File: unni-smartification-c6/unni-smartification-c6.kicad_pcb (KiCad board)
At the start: 2 copper layers, 83.3 x 65 mm, 73 parts, among them J1 USB-C (replacement daughterbo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, J10 UART TEST, J2 Li-Ion 1S JST-PH, J20 CO2 tap: SDA/SCL/GND, J21 RT/RH tap: RT/RH/GND, J22 TOUCH / LED+ / LED- / GND, J4 UNNI DC / battery input - AC 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, Q1 AO3401A, Q10 AO3400A touch emulator, Q2 AO3401A, Q3 AO3400A, Q4 AO3400A, U1 MCP73831T-2ACI/OT, U10 ESP32-C6-MINI-1, U2 TPS63031DSK, U3 TPS613222ADBZ (5V)

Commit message: trying routing the usb-pcb
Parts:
- added U4: USBLC6-2SC6, Package_TO_SOT_SMD:SOT-23-6, B.Cu at (0.00, 0.00)
- D1, D3, D4: footprint Diode_SMD:D_SMA -> Diode_SMD:D_SMA_Handsoldering
- Q1, Q10, Q2, Q3, Q4, U3: footprint Package_TO_SOT_SMD:SOT-23 -> Package_TO_SOT_SMD:SOT-23_Handsoldering
- U1: footprint Package_TO_SOT_SMD:SOT-23-5 -> Package_TO_SOT_SMD:SOT-23-5_HandSoldering
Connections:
- J1 pad A6: USB_RAW_P -> USB_P
- J1 pad A7: USB_RAW_N -> USB_N
- J1 pad B6: USB_RAW_P -> USB_P
- J1 pad B7: USB_RAW_N -> USB_N
- J2 pad 1: +BATT -> GND
- J2 pad 2: GND -> +BATT
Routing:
- net VBUS: track 0.00 -> 17.4 mm, vias 0 -> 14
- net Net-(Q3-G): track 0.00 -> 10.6 mm
- net SYS: track 0.00 -> 10.6 mm, vias 0 -> 2
- net USB_N: track 0.00 -> 9.54 mm
- net USB_P: track 0.00 -> 8.87 mm
- net +BATT: track 0.00 -> 8.37 mm, vias 0 -> 14
- net Net-(Q2-G): track 0.00 -> 7.80 mm
- net /USB + Power/BOOST_IN: track 0.00 -> 7.66 mm, vias 0 -> 6
- net Net-(Q1-G): track 0.00 -> 7.54 mm
- net +3V3: track 0.00 -> 4.00 mm, vias 0 -> 2
- net GND: track 0.00 -> 3.67 mm, vias 0 -> 22
- net Net-(U1-PROG): track 0.00 -> 2.22 mm
- net Net-(J1-CC1): track 7.64 -> 9.80 mm
- net Net-(J1-CC2): track 7.39 -> 9.43 mm
- net Net-(U1-STAT): track 0.00 -> 1.97 mm
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- added copper zone on B.Cu, net +BATT
- added copper zone on F.Cu, net +BATT
- added copper zone on B.Cu, net /USB + Power/BOOST_IN
- added copper zone on F.Cu, net Net-(U2-L1)
- added copper zone on F.Cu, net Net-(U2-L2)
- added copper zone on F.Cu, net Net-(U3-SW)
- added copper zone on B.Cu, net SYS
- added copper zone on B.Cu, net VBUS
- added copper zone on F.Cu, net VBUS

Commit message: add usb-esp and finalize usb-pcb
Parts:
- added C14: 100n, Capacitor_SMD:C_0603_1608Metric_Pad1.08x0.95mm_HandSolder, B.Cu at (0.00, 0.00)
- C9: moved to B.Cu
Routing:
- net +BATT: track 8.37 -> 0.00 mm, vias 14 -> 13
- net Net-(Q2-G): track 7.80 -> 0.00 mm
- net /USB + Power/BOOST_IN: track 7.66 -> 0.00 mm, vias 6 -> 12
- net UNNI_AC: track 0.00 -> 3.54 mm, vias 0 -> 1
- net Net-(Q3-G): track 10.6 -> 13.8 mm
- net GND: track 3.67 -> 6.22 mm, vias 22 -> 38
- net VBUS: track 17.4 -> 19.8 mm, vias 14 -> 20
- net Net-(J1-CC1): track 9.80 -> 11.0 mm
- net Net-(J1-CC2): track 9.43 -> 8.64 mm
- net USB_P: track 8.87 -> 8.15 mm
- added copper zone on In1.Cu, net GND
- added copper zone on In2.Cu, net GND
- added copper zone on F.Cu, net Net-(Q2-G)
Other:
- copper layers 2 -> 4

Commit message: move some power stuff to esp board, update some footprints
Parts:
- added SW1: RESET, Button_Switch_THT:SW_PUSH_6mm, F.Cu at (0.00, 0.00)
- added SW2: BOOT, Button_Switch_THT:SW_PUSH_6mm, F.Cu at (0.00, 0.00)
- C9: moved to F.Cu
- J2: footprint Connector_JST:JST_PH_S2B-PH-SM4-TB_1x02-1MP_P2.00mm_Horizontal -> Connector_JST:JST_PH_S2B-PH-K_1x02_P2.00mm_Horizontal
- L1: value 1.5uH -> 2.2uH
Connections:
- J4 pad 2: UNNI_AC -> GND
- J4 pad 3: GND -> UNNI_AC
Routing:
- net +BATT: track 0.00 -> 13.9 mm
- net SYS: track 10.9 -> 5.99 mm
- net UNNI_AC: track 3.54 -> 0.00 mm, vias 1 -> 0
- net Net-(Q1-G): track 7.76 -> 4.58 mm
- net VBUS: track 19.8 -> 21.2 mm, vias 20 -> 33
- net Net-(Q3-G): track 13.8 -> 12.5 mm, vias 0 -> 2
- net GND: track 6.22 -> 5.61 mm, vias 38 -> 51
- net /USB + Power/BOOST_IN: vias 12 -> 0
- added copper zone on F.Cu, net UNNI_AC

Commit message: re-do ESP PCB
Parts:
- removed J10: UART TEST, Connector_JST:JST_PH_S3B-PH-SM4-TB_1x03-1MP_P2.00mm_Horizontal
- removed J20: CO2 tap: SDA/SCL/GND, Connector_JST:JST_PH_S3B-PH-SM4-TB_1x03-1MP_P2.00mm_Horizontal
- removed J21: RT/RH tap: RT/RH/GND, Connector_JST:JST_PH_S3B-PH-SM4-TB_1x03-1MP_P2.00mm_Horizontal
- removed J22: TOUCH / LED+ / LED- / GND, Connector_JST:JST_PH_S4B-PH-SM4-TB_1x04-1MP_P2.00mm_Horizontal
- removed TP1: BACKLIGHT_LED_NEG, TestPoint:TestPoint_Pad_D1.0mm
- added J11, J24, J3: Conn_01x01, Connector_Wire:SolderWire-0.5sqmm_1x01_D0.9mm_OD2.1mm, F.Cu at (0.00, 0.00)
- added J12, J13, J14, J15, J17, J18, J19, J23, J25, J26, J27, J5, J6, J7, J8, J9: Conn_01x01, Connector_Wire:SolderWire-0.1sqmm_1x01_D0.4mm_OD1mm, F.Cu at (0.00, 0.00)
- L1: footprint Inductor_SMD:L_TDK_NLV32_3.2x2.5mm -> Unni_Inductor:L_Murata_LQH3NPN_3.0x3.0mm_HandSolder
- L2: footprint Inductor_SMD:L_TDK_NLV32_3.2x2.5mm -> Unni_Inductor:L_Murata_DFE322520FD_3.2x2.5mm_HandSolder
- RT1: footprint Resistor_THT:R_Axial_DIN0204_L3.6mm_D1.6mm_P5.08mm_Horizontal -> Connector_PinSocket_2.54mm:PinSocket_1x02_P2.54mm_Vertical
- SW1, SW2: footprint Button_Switch_THT:SW_PUSH_6mm -> Unni_Switch:SW_Jianfu_TVAF36-N014JW-R_HandSolder
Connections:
- net GND renamed CONN_GND
- net Net-(J22-Pin_1) renamed CONN_TOUCH
- net USB_N renamed USBPort_N
- net USB_P renamed USBPort_P
- net USB_RAW_N renamed CONN_USB_N
- net USB_RAW_P renamed CONN_USB_P
- net VBUS renamed CONN_VBUS
- R40 pad 1: Net-(J20-Pin_1) -> CONN_SDA
- R41 pad 1: Net-(J20-Pin_2) -> CONN_SCL
- R42 pad 1: Net-(J21-Pin_1) -> CONN_RT
- R43 pad 1: Net-(J21-Pin_2) -> CONN_RH
- R50 pad 1: Net-(J22-Pin_2) -> CONN_LED+
- U10 pad 30: Net-(J10-Pin_1) -> unconnected-(U10-RXD0-Pad30)
- U10 pad 31: Net-(J10-Pin_2) -> unconnected-(U10-TXD0-Pad31)
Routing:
- net BOOST_CMD: track 0.00 -> 67.3 mm, vias 0 -> 1
- net CONN_USB_P: track 0.00 -> 63.8 mm
- net CONN_USB_N: track 0.00 -> 63.0 mm
- net CHARGE_STAT: track 1.89 -> 34.7 mm, vias 0 -> 2
- net BAT_TEMP_ADC: track 0.00 -> 30.0 mm, vias 0 -> 1
- net CONN_GND: track 5.61 -> 31.7 mm, vias 51 -> 50
- net TOUCH_TRIGGER: track 0.00 -> 22.2 mm, vias 0 -> 4
- net RH: track 0.00 -> 17.4 mm, vias 0 -> 2
- net RT: track 0.00 -> 15.1 mm, vias 0 -> 2
- net BACKLIGHT_ADC: track 0.00 -> 14.7 mm, vias 0 -> 2
- net +3V3: track 4.00 -> 17.1 mm, vias 2 -> 13
- net CONN_VBUS: track 21.2 -> 32.9 mm, vias 33 -> 30
- net /ESP32-C6 + Auxiliary/ESP_EN: track 0.00 -> 10.9 mm
- net /ESP32-C6 + Auxiliary/USB_P: track 0.00 -> 9.76 mm
- net /ESP32-C6 + Auxiliary/USB_N: track 0.00 -> 9.76 mm
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- added copper zone on B.Cu, net +3V3
- removed copper zone on B.Cu, net SYS

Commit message: Clean up power nets and routing rules
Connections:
- net CONN_GND renamed GND
- net CONN_USB_N renamed USB_RAW_N
- net CONN_USB_P renamed USB_RAW_P
- net CONN_VBUS renamed VBUS

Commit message: new tvs diode, final fiddlings
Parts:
- removed C14: 100n, Capacitor_SMD:C_0603_1608Metric_Pad1.08x0.95mm_HandSolder
- removed J11, J24: Conn_01x01, Connector_Wire:SolderWire-0.5sqmm_1x01_D0.9mm_OD2.1mm
- removed J12, J13, J14, J15, J17, J18, J19, J23, J25, J26, J27, J7, J8, J9: Conn_01x01, Connector_Wire:SolderWire-0.1sqmm_1x01_D0.4mm_OD1mm
- added C22: 100nF, Capacitor_SMD:C_0603_1608Metric_Pad1.08x0.95mm_HandSolder, F.Cu at (0.00, 0.00)
- added J10: Conn_01x06, Connector_JST:JST_PH_B6B-PH-K_1x06_P2.00mm_Vertical, F.Cu at (0.00, 0.00)
- J2: footprint Connector_JST:JST_PH_S2B-PH-K_1x02_P2.00mm_Horizontal -> Connector_JST:JST_PH_B2B-PH-K_1x02_P2.00mm_Vertical
- J3: value Conn_01x01 -> Conn_01x06; footprint Connector_Wire:SolderWire-0.5sqmm_1x01_D0.9mm_OD2.1mm -> Connector_JST:JST_PH_B6B-PH-K_1x06_P2.00mm_Vertical
- J5: value Conn_01x01 -> Conn_01x02; footprint Connector_Wire:SolderWire-0.1sqmm_1x01_D0.4mm_OD1mm -> Connector_JST:JST_PH_B2B-PH-K_1x02_P2.00mm_Vertical
- J6: value Conn_01x01 -> Conn_01x05; footprint Connector_Wire:SolderWire-0.1sqmm_1x01_D0.4mm_OD1mm -> Connector_JST:JST_PH_B5B-PH-K_1x05_P2.00mm_Vertical
- R3: value 3.3k -> 5.1k
- R40, R41, R42, R43: footprint Resistor_SMD:R_0805_2012Metric_Pad1.20x1.40mm_HandSolder -> Resistor_SMD:R_0603_1608Metric_Pad0.98x0.95mm_HandSolder
- RT1: footprint Connector_PinSocket_2.54mm:PinSocket_1x02_P2.54mm_Vertical -> Connector_JST:JST_PH_B2B-PH-K_1x02_P2.00mm_Vertical
- U4: value USBLC6-2SC6 -> TPD2E009DBZR; footprint Package_TO_SOT_SMD:SOT-23-6 -> Package_TO_SOT_SMD:SOT-23_Handsoldering
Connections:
- J1 pad A6: USBPort_P -> USB_RAW_P
- J1 pad A7: USBPort_N -> USB_RAW_N
- J1 pad B6: USBPort_P -> USB_RAW_P
- J1 pad B7: USBPort_N -> USB_RAW_N
- J3 pad 1: GND -> USB_RAW_P
- J5 pad 1: BOOST_CMD -> CONN_TOUCH
- J6 pad 1: VBUS -> CONN_SCL
- U4 pad 1: USBPort_N -> USB_RAW_P
- U4 pad 2: GND -> USB_RAW_N
- U4 pad 3: USBPort_P -> GND
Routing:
- net USB_RAW_P: track 63.8 -> 15.8 mm
- net USB_RAW_N: track 63.0 -> 16.3 mm
- net VBUS: track 32.9 -> 18.0 mm, vias 30 -> 47
- net USBPort_N: track 9.46 -> 0.00 mm
- net USB_ADC: track 0.00 -> 9.33 mm
- net USBPort_P: track 8.15 -> 0.00 mm
- net TOUCH_TRIGGER: track 22.2 -> 28.8 mm
- net CHARGE_STAT: track 34.7 -> 41.1 mm
- net +BATT: track 10.8 -> 16.5 mm, vias 13 -> 31
- net CO2_SCL: track 9.64 -> 4.42 mm
- net BAT_TEMP_EXCITE: track 2.57 -> 7.67 mm
- net RH: track 17.4 -> 12.7 mm, vias 2 -> 4
- net BACKLIGHT_ADC: track 14.7 -> 11.7 mm
- net CONN_RT: track 2.21 -> 5.26 mm
- net CONN_RH: track 2.17 -> 5.03 mm
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- added copper zone on B.Cu, net SYS

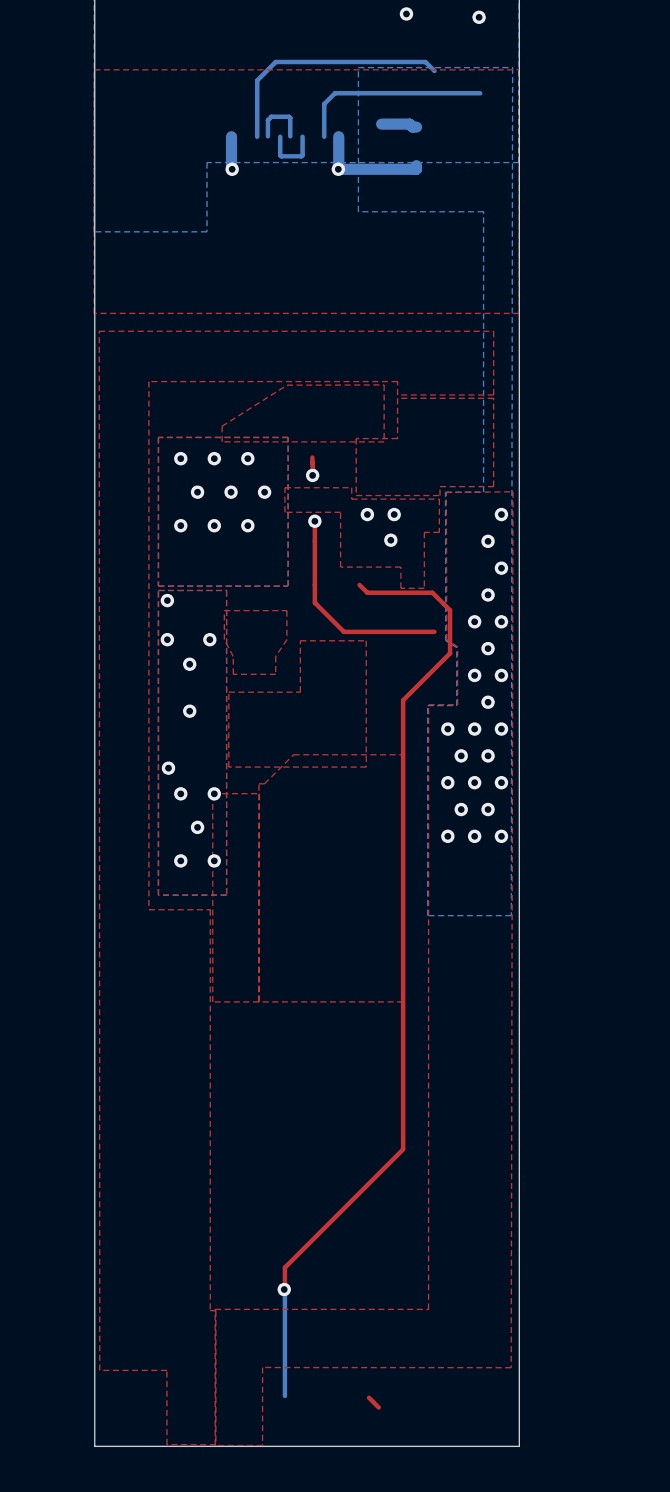
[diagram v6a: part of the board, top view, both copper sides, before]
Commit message: Align stackup and validation with JLCPCB
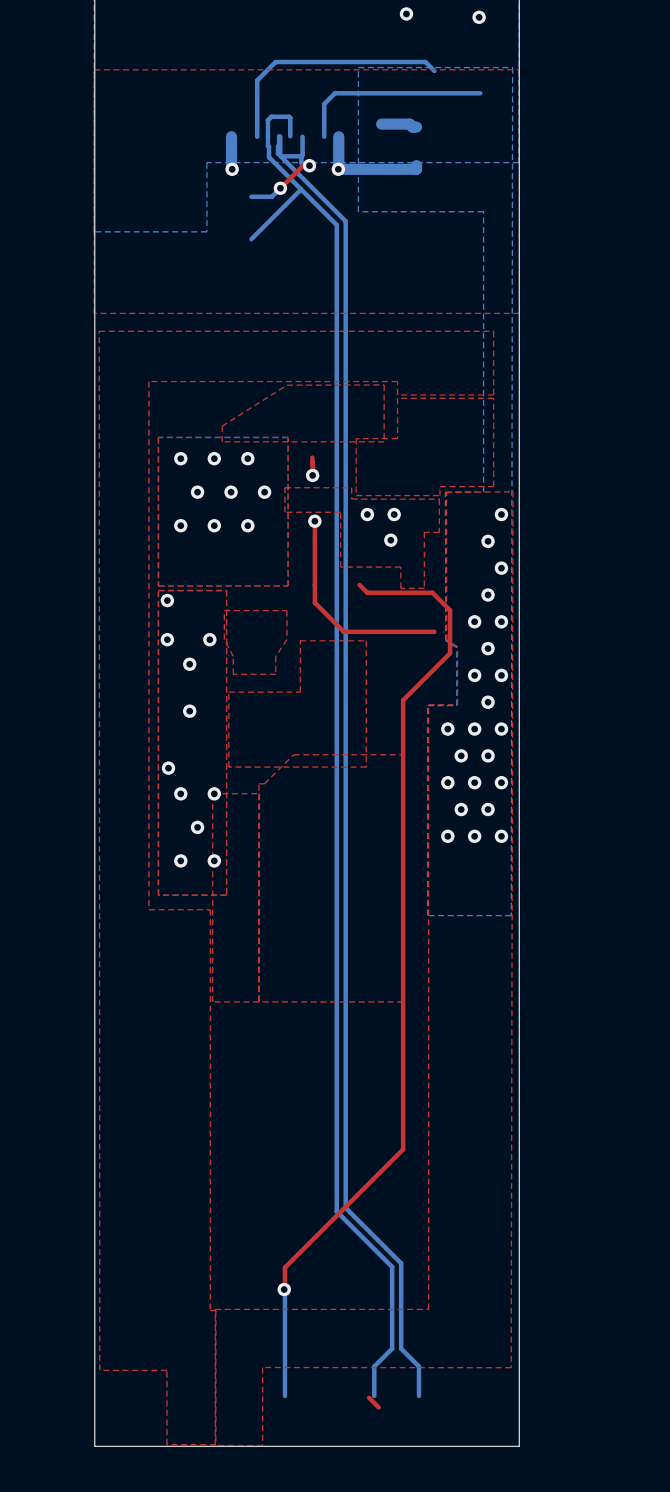
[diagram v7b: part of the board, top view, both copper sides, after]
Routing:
- net USB_RAW_P: track 15.8 -> 78.7 mm, vias 0 -> 2
- net USB_RAW_N: track 16.3 -> 78.5 mm

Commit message: cleanups, silkscreen
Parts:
- removed C30: 47pF DNP, Capacitor_SMD:C_0603_1608Metric_Pad1.08x0.95mm_HandSolder
- removed C31: 100pF DNP, Capacitor_SMD:C_0603_1608Metric_Pad1.08x0.95mm_HandSolder
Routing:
- net CONN_TOUCH: track 6.20 -> 3.31 mm
